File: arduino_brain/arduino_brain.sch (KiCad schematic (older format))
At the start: 49 parts, among them Q1 2N3904, Q10 2N3904, Q11 2N3906, Q2 TIP120, Q3 TIP120, Q4 2N3904, Q5 2N3906, Q6 2N3904, Q7 2N3906, Q8 2N3904, Q9 2N3906, U2 CRE1S2412SC

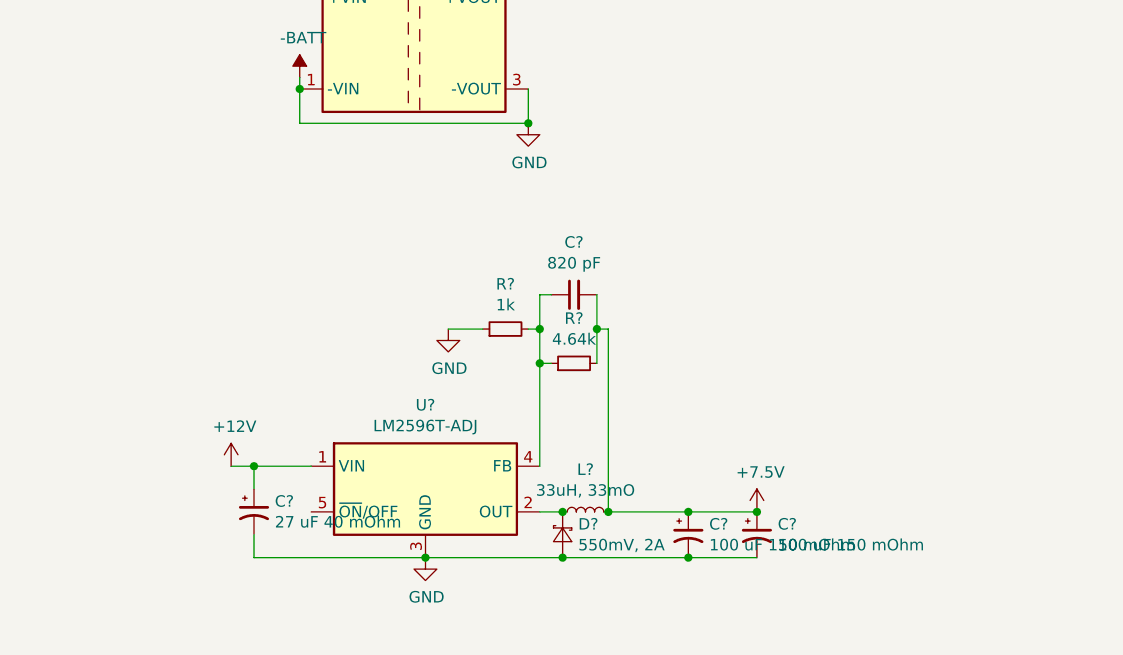
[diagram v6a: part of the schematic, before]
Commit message: Implemented components for 12 to 7 V buck
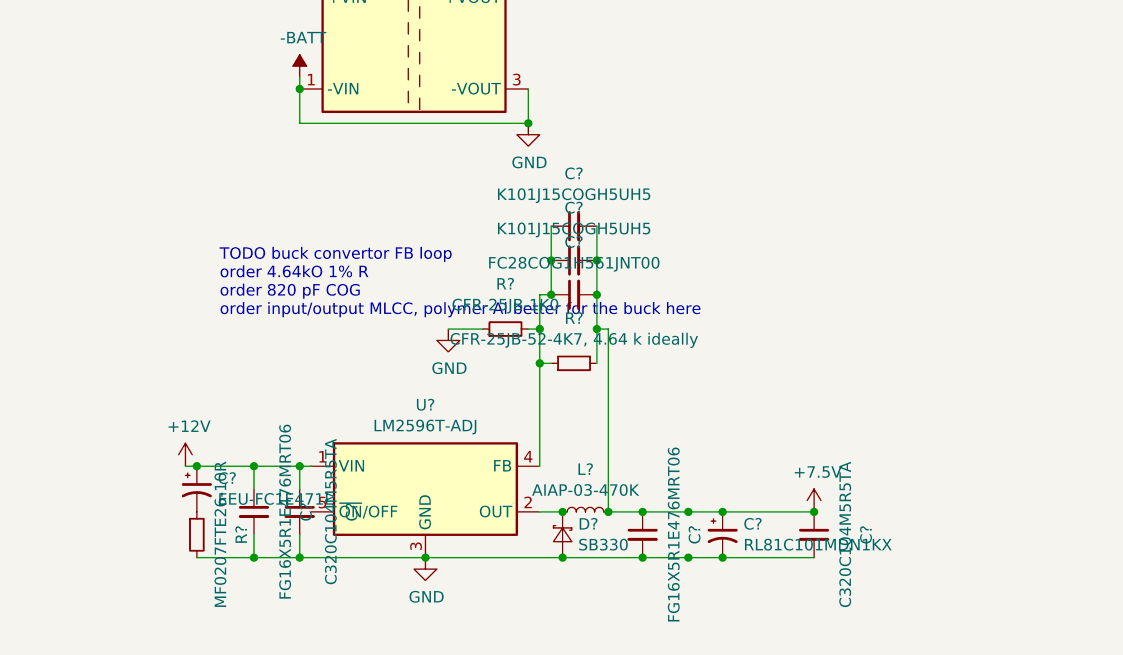
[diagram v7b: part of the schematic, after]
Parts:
- removed C?: 100 uF 150 mOhm, symbol Device:CP1_Small
- added C? (x2): C320C104M5R5TA, symbol Device:C_Small
- added C? (x2): FG16X5R1E476MRT06, symbol Device:C_Small
- added C? (x2): K101J15COGH5UH5, symbol Device:C_Small
- added R?: MF0207FTE26-10R, symbol Device:R_Small
- C?: value 27 uF 40 mOhm -> EEU-FC1E471L
- C?: value 820 pF -> FC28COG1H561JNT00
- C?: value 100 uF 150 mOhm -> RL81C101MDN1KX
- D?: value 550mV, 2A -> SB330
- L?: value 33uH, 33mO -> AIAP-03-470K
- R?: value 1k -> CFR-25JB-1K0
- R?: value 4.64k -> CFR-25JB-52-4K7, 4.64 k ideally
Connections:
- net +12V: now also C?.1, C?.1
- net +7.5V: now also C?.1, C?.1, C?.2, C?.2
- net -BATT: now also C?.2, C?.2, C?.2, C?.2, R?.2; no longer C?.2
- net at C?.1, R?.1, R?.2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: now also C?.1, C?.1
- new net: C?.2, R?.1
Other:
- note added: "TODO buck convertor FB loop\norder 4.64kO 1% R\norder 820 pF COG\norder input/output MLCC, polymer Al better for the buck here"
- moved on the sheet: C?
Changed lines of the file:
@@
 L power:+12V #PWR0107
 U 1 1 5E107F0F
-P 750 10550
-F 0 "#PWR0107" H 750 10400 50  0001 C CNN
-F 1 "+12V" H 765 10723 50  0000 C CNN
-F 2 "" H 750 10550 50  0001 C CNN
-F 3 "" H 750 10550 50  0001 C CNN
-	1    750  10550
+P 550 10550
+F 0 "#PWR0107" H 550 10400 50  0001 C CNN
+F 1 "+12V" H 565 10723 50  0000 C CNN
+F 2 "" H 550 10550 50  0001 C CNN
+F 3 "" H 550 10550 50  0001 C CNN
+	1    550  10550
 	1    0    0    -1
 $EndComp
@@
 L Device:CP1_Small C?
 U 1 1 5EA898FE
-P 850 10750
-F 0 "C?" H 941 10796 50  0000 L CNN
-F 1 "27 uF 40 mOhm" H 941 10705 50  0000 L CNN
-F 2 "" H 850 10750 50  0001 C CNN
-F 3 "~" H 850 10750 50  0001 C CNN
-	1    850  10750
-	1    0    0    -1
-$EndComp
-Wire Wire Line
-	850  10850 850  10950
-Wire Wire Line
-	850  10950 1600 10950
+P 600 10650
+F 0 "C?" H 691 10696 50  0000 L CNN
+F 1 "EEU-FC1E471L" H 691 10605 50  0000 L CNN
+F 2 "" H 600 10650 50  0001 C CNN
+F 3 "~" H 600 10650 50  0001 C CNN
+	1    600  10650
+	1    0    0    -1
+$EndComp
+Wire Wire Line
+	600  10950 850  10950
 Connection ~ 1600 10950
-Wire Wire Line
-	750  10550 850  10550
-Wire Wire Line
-	850  10550 850  10650
-Connection ~ 850  10550
-Wire Wire Line
-	850  10550 1100 10550
 $Comp
 L Device:C_Small C?
@@
 P 2250 9800
 F 0 "C?" V 2479 9800 50  0000 C CNN
-F 1 "820 pF" V 2388 9800 50  0000 C CNN
+F 1 "FC28COG1H561JNT00" V 2388 9800 50  0000 C CNN
 F 2 "" H 2250 9800 50  0001 C CNN
 F 3 "~" H 2250 9800 50  0001 C CNN
@@
 P 1950 9950
 F 0 "R?" V 2146 9950 50  0000 C CNN
-F 1 "1k" V 2055 9950 50  0000 C CNN
+F 1 "CFR-25JB-1K0" V 2055 9950 50  0000 C CNN
 F 2 "" H 1950 9950 50  0001 C CNN
 F 3 "~" H 1950 9950 50  0001 C CNN
@@
 P 2250 10100
 F 0 "R?" V 2446 10100 50  0000 C CNN
-F 1 "4.64k" V 2355 10100 50  0000 C CNN
+F 1 "CFR-25JB-52-4K7, 4.64 k ideally" V 2355 10100 50  0000 C CNN
 F 2 "" H 2250 10100 50  0001 C CNN
 F 3 "~" H 2250 10100 50  0001 C CNN
@@
 P 2200 10850
 F 0 "D?" V 2154 10782 50  0000 R CNN
-F 1 "550mV, 2A" V 2245 10782 50  0000 R CNN
+F 1 "SB330" V 2245 10782 50  0000 R CNN
 F 2 "" V 2200 10850 50  0001 C CNN
 F 3 "~" V 2200 10850 50  0001 C CNN
@@
 P 2300 10750
 F 0 "L?" V 2485 10750 50  0000 C CNN
-F 1 "33uH, 33mO" V 2394 10750 50  0000 C CNN
+F 1 "AIAP-03-470K" V 2394 10750 50  0000 C CNN
 F 2 "" H 2300 10750 50  0001 C CNN
 F 3 "~" H 2300 10750 50  0001 C CNN
@@
 L Device:CP1_Small C?
 U 1 1 5EB2E9E9
-P 2750 10850
-F 0 "C?" H 2841 10896 50  0000 L CNN
-F 1 "100 uF 150 mOhm" H 2841 10805 50  0000 L CNN
-F 2 "" H 2750 10850 50  0001 C CNN
-F 3 "~" H 2750 10850 50  0001 C CNN
-	1    2750 10850
-	1    0    0    -1
-$EndComp
-$Comp
-L Device:CP1_Small C?
-U 1 1 5EB2F8A1
-P 3050 10850
-F 0 "C?" H 3141 10896 50  0000 L CNN
-F 1 "100 uF 150 mOhm" H 3141 10805 50  0000 L CNN
-F 2 "" H 3050 10850 50  0001 C CNN
-F 3 "~" H 3050 10850 50  0001 C CNN
-	1    3050 10850
-	1    0    0    -1
-$EndComp
-Wire Wire Line
-	2400 10750 2750 10750
+P 2900 10850
+F 0 "C?" H 2991 10896 50  0000 L CNN
+F 1 "RL81C101MDN1KX" H 2991 10805 50  0000 L CNN
+F 2 "" H 2900 10850 50  0001 C CNN
+F 3 "~" H 2900 10850 50  0001 C CNN
+	1    2900 10850
+	1    0    0    -1
+$EndComp
+Wire Wire Line
+	2400 10750 2550 10750
 Connection ~ 2400 10750
-Wire Wire Line
-	2750 10750 3050 10750
 Connection ~ 2750 10750
 Wire Wire Line
-	2200 10950 2750 10950
+	2200 10950 2550 10950
 Connection ~ 2200 10950
-Wire Wire Line
-	3050 10950 2750 10950
 Connection ~ 2750 10950
 $Comp
@@
 L power:+7.5V #PWR?
 U 1 1 5EB62DBD
-P 3050 10750
-F 0 "#PWR?" H 3050 10600 50  0001 C CNN
-F 1 "+7.5V" H 3065 10923 50  0000 C CNN
-F 2 "" H 3050 10750 50  0001 C CNN
-F 3 "" H 3050 10750 50  0001 C CNN
-	1    3050 10750
-	1    0    0    -1
-$EndComp
-Connection ~ 3050 10750
+P 3300 10750
+F 0 "#PWR?" H 3300 10600 50  0001 C CNN
+F 1 "+7.5V" H 3315 10923 50  0000 C CNN
+F 2 "" H 3300 10750 50  0001 C CNN
+F 3 "" H 3300 10750 50  0001 C CNN
+	1    3300 10750
+	1    0    0    -1
+$EndComp
+Connection ~ 3300 10750
 $Comp
 L power:+7.5V #PWR?
@@
 Text Notes -1750 4350 2    50   ~ 0
 taillight
+$Comp
+L Device:C_Small C?
+U 1 1 5E389EAC
+P 1050 10750
+F 0 "C?" V 1279 10750 50  0000 C CNN
+F 1 "C320C104M5R5TA" V 1188 10750 50  0000 C CNN
+F 2 "" H 1050 10750 50  0001 C CNN
+F 3 "~" H 1050 10750 50  0001 C CNN
+	1    1050 10750
+	1    0    0    -1
+$EndComp
+Wire Wire Line
+	1050 10950 1600 10950
+$Comp
+L Device:C_Small C?
+U 1 1 5E3DC369
+P 850 10750
+F 0 "C?" V 1079 10750 50  0000 C CNN
+F 1 "FG16X5R1E476MRT06" V 988 10750 50  0000 C CNN
+F 2 "" H 850 10750 50  0001 C CNN
+F 3 "~" H 850 10750 50  0001 C CNN
+	1    850  10750
+	1    0    0    -1
+$EndComp
+Wire Wire Line
+	850  10650 850  10550
+Connection ~ 850  10550
+Wire Wire Line
+	850  10850 850  10950
+Connection ~ 850  10950
+Wire Wire Line
+	850  10950 1050 10950
+Wire Wire Line
+	550  10550 600  10550
+Connection ~ 600  10550
+Wire Wire Line
+	600  10550 850  10550
+$Comp
+L Device:R_Small R?
+U 1 1 5E3F5204
+P 600 10850
+F 0 "R?" V 796 10850 50  0000 C CNN
+F 1 "MF0207FTE26-10R" V 705 10850 50  0000 C CNN
+F 2 "" H 600 10850 50  0001 C CNN
+F 3 "~" H 600 10850 50  0001 C CNN
+	1    600  10850
+	1    0    0    -1
+$EndComp
+$Comp
+L Device:C_Small C?
+U 1 1 5E40EDD4
+P 3300 10850
+F 0 "C?" V 3529 10850 50  0000 C CNN
+F 1 "C320C104M5R5TA" V 3438 10850 50  0000 C CNN
+F 2 "" H 3300 10850 50  0001 C CNN
+F 3 "~" H 3300 10850 50  0001 C CNN
+	1    3300 10850
+	1    0    0    -1
+$EndComp
+Text Notes 700  9900 0    50   ~ 0
+TODO buck convertor FB loop\norder 4.64kO 1% R\norder 820 pF COG\norder input/output MLCC, polymer Al better for the buck here
+$Comp
+L Device:C_Small C?
+U 1 1 5E40FEC5
+P 2250 9500
+F 0 "C?" V 2479 9500 50  0000 C CNN
+F 1 "K101J15COGH5UH5" V 2388 9500 50  0000 C CNN
+F 2 "" H 2250 9500 50  0001 C CNN
+F 3 "~" H 2250 9500 50  0001 C CNN
+	1    2250 9500
+	0    -1   -1   0
+$EndComp
+$Comp
+L Device:C_Small C?
+U 1 1 5E41038E
+P 2250 9650
+F 0 "C?" V 2479 9650 50  0000 C CNN
+F 1 "K101J15COGH5UH5" V 2388 9650 50  0000 C CNN
+F 2 "" H 2250 9650 50  0001 C CNN
+F 3 "~" H 2250 9650 50  0001 C CNN
+	1    2250 9650
+	0    -1   -1   0
+$EndComp
+Wire Wire Line
+	2350 9800 2350 9650
+Connection ~ 2350 9800
+Wire Wire Line
+	2350 9650 2350 9500
+Connection ~ 2350 9650
+Wire Wire Line
+	2150 9500 2150 9650
+Wire Wire Line
+	2150 9650 2150 9800
+Connection ~ 2150 9650
+Connection ~ 2150 9800
+Connection ~ 1050 10950
+Wire Wire Line
+	1050 10850 1050 10950
+Wire Wire Line
+	850  10550 1050 10550
+Wire Wire Line
+	1050 10650 1050 10550
+Connection ~ 1050 10550
+Wire Wire Line
+	1050 10550 1100 10550
+$Comp
+L Device:C_Small C?
+U 1 1 5E491E51
+P 2550 10850
+F 0 "C?" V 2779 10850 50  0000 C CNN
+F 1 "FG16X5R1E476MRT06" V 2688 10850 50  0000 C CNN
+F 2 "" H 2550 10850 50  0001 C CNN
+F 3 "~" H 2550 10850 50  0001 C CNN
+	1    2550 10850
+	1    0    0    -1
+$EndComp
+Connection ~ 2550 10750
+Connection ~ 2550 10950
+Wire Wire Line
+	2750 10750 2900 10750
+Wire Wire Line
+	2750 10950 2900 10950
+Connection ~ 2900 10750
+Wire Wire Line
+	2900 10750 3300 10750
+Connection ~ 2900 10950
+Wire Wire Line
+	2900 10950 3300 10950
+Wire Wire Line
+	2550 10950 2750 10950
+Wire Wire Line
+	2550 10750 2750 10750
 $EndSCHEMATC

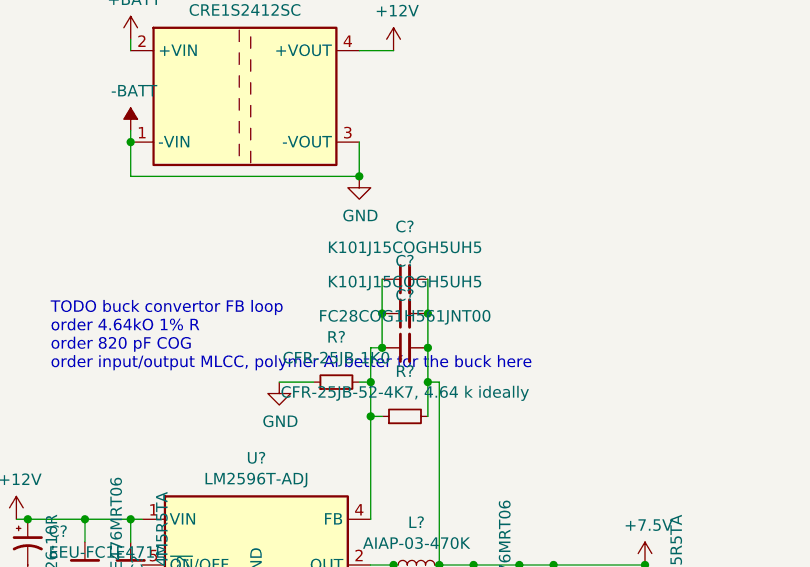
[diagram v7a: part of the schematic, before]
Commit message: Switching regulator with components as selected from EE tutorial - not working
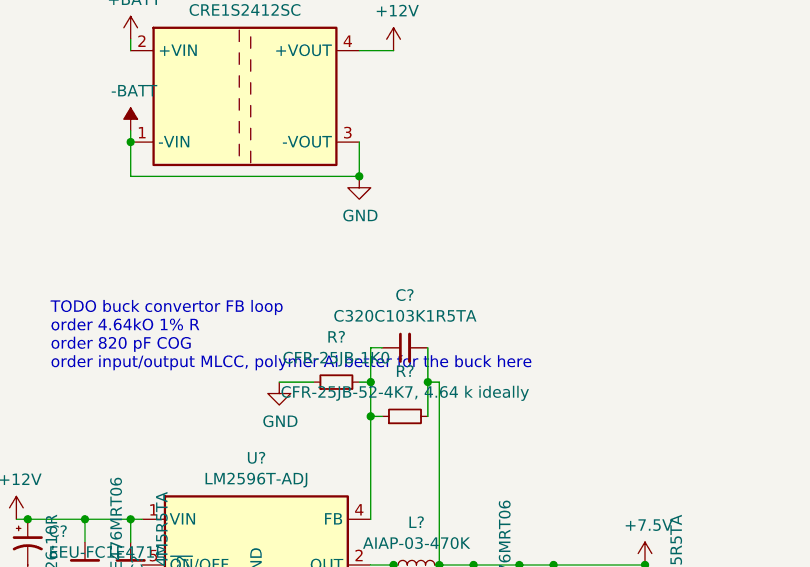
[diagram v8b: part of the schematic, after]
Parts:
- removed C? (x2): K101J15COGH5UH5, symbol Device:C_Small
- C?: value FC28COG1H561JNT00 -> C320C103K1R5TA
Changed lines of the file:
@@
 P 2250 9800
 F 0 "C?" V 2479 9800 50  0000 C CNN
-F 1 "FC28COG1H561JNT00" V 2388 9800 50  0000 C CNN
+F 1 "C320C103K1R5TA" V 2388 9800 50  0000 C CNN
 F 2 "" H 2250 9800 50  0001 C CNN
 F 3 "~" H 2250 9800 50  0001 C CNN
@@
 Text Notes 700  9900 0    50   ~ 0
 TODO buck convertor FB loop\norder 4.64kO 1% R\norder 820 pF COG\norder input/output MLCC, polymer Al better for the buck here
-$Comp
-L Device:C_Small C?
-U 1 1 5E40FEC5
-P 2250 9500
-F 0 "C?" V 2479 9500 50  0000 C CNN
-F 1 "K101J15COGH5UH5" V 2388 9500 50  0000 C CNN
-F 2 "" H 2250 9500 50  0001 C CNN
-F 3 "~" H 2250 9500 50  0001 C CNN
-	1    2250 9500
-	0    -1   -1   0
-$EndComp
-$Comp
-L Device:C_Small C?
-U 1 1 5E41038E
-P 2250 9650
-F 0 "C?" V 2479 9650 50  0000 C CNN
-F 1 "K101J15COGH5UH5" V 2388 9650 50  0000 C CNN
-F 2 "" H 2250 9650 50  0001 C CNN
-F 3 "~" H 2250 9650 50  0001 C CNN
-	1    2250 9650
-	0    -1   -1   0
-$EndComp
-Wire Wire Line
-	2350 9800 2350 9650
-Connection ~ 2350 9800
-Wire Wire Line
-	2350 9650 2350 9500
-Connection ~ 2350 9650
-Wire Wire Line
-	2150 9500 2150 9650
-Wire Wire Line
-	2150 9650 2150 9800
-Connection ~ 2150 9650
-Connection ~ 2150 9800
 Connection ~ 1050 10950
 Wire Wire Line
